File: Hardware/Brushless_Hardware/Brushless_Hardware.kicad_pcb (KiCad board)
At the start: 2 copper layers, 134.8 x 71.8 mm, 101 parts, among them J1 RJ45_LED_Shielded, SW1 SW_Push, SW2 SW_Push, SW3 SW_Push, SW4 SW_Push, SW5 SW_Push, SW6 SW_Push, SW7 SW_DPDT_x2, U1 Teensy4.1_DEV-16771, U2 OKI, U3 TSR_1-2450

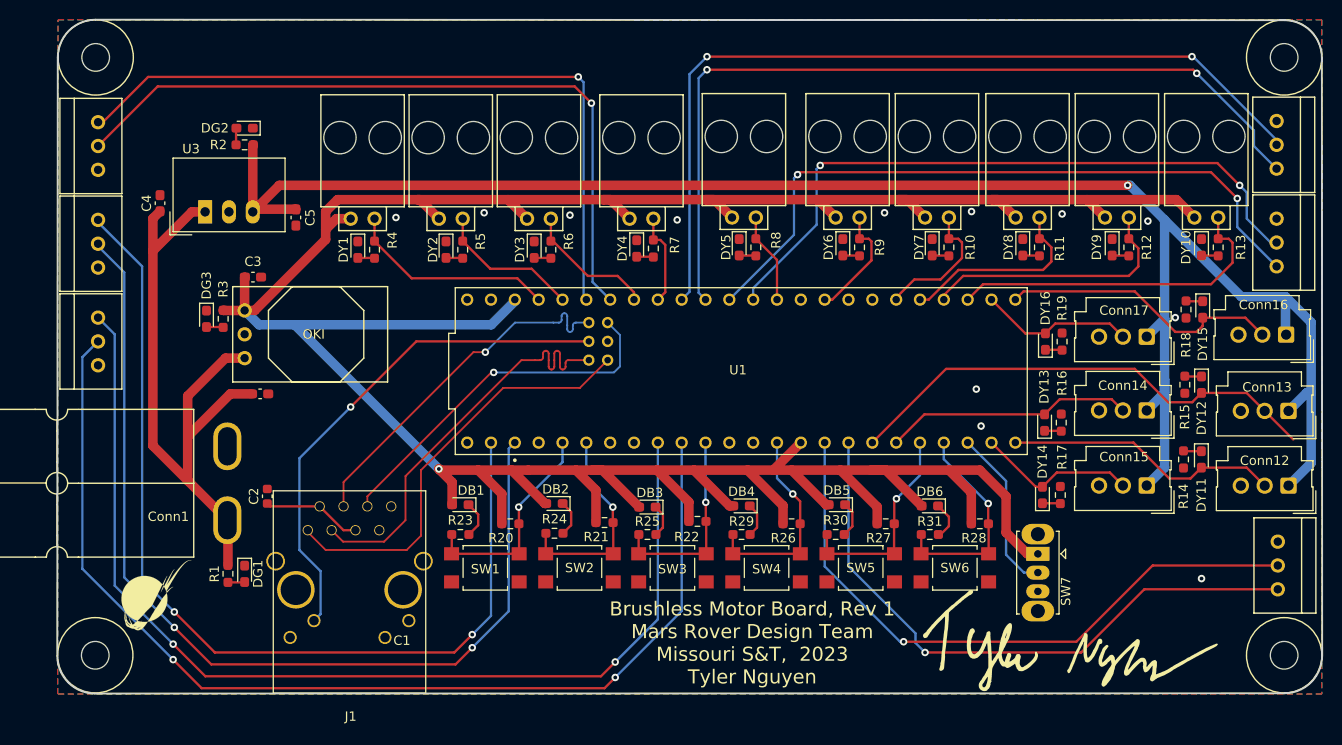
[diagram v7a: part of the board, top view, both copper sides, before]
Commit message: Replaced connectors and did more labeling
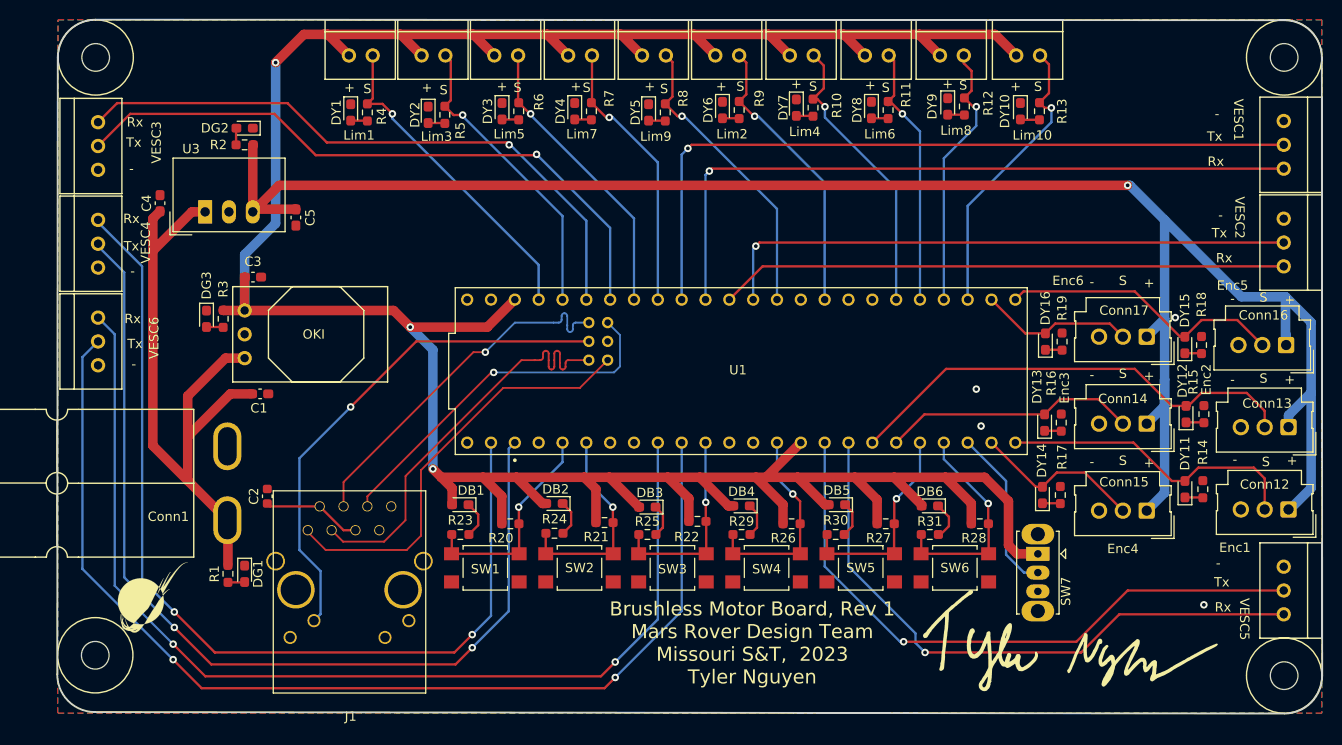
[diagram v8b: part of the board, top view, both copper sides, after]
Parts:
- Conn10, Conn11, Conn2, Conn3, Conn4, Conn5, Conn6, Conn7, Conn8, Conn9: footprint MRDT_Connectors:MOLEX_SL_02_Horizontal -> MRDT_Connectors:MOLEX_SL_02_Vertical
- moved Conn11 25.7 mm to (156.1, 28.1)
- moved Conn10 24.7 mm to (148.0, 28.1)
- moved DY10 24.1 mm to (156.6, 34.0)
- moved R13 23.9 mm to (158.6, 34.0)
- moved Conn9 23.6 mm to (140.0, 28.1)
- moved DY9 23.1 mm to (148.8, 33.5)
- moved R12 23.1 mm to (150.6, 33.5)
- moved Conn8 22.5 mm to (132.0, 28.1)
- moved DY8 21.8 mm to (140.7, 33.9)
- moved R11 21.8 mm to (142.5, 33.9)
- moved Conn7 21.5 mm to (124.1, 28.1)
- moved DY7 20.8 mm to (132.7, 33.6)
- moved R10 20.8 mm to (134.5, 33.6)
- moved Conn6 19.8 mm to (116.3, 28.1)
- moved DY6 19.5 mm to (124.8, 33.9)
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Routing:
- net LIM_9: track 9.68 -> 32.0 mm, vias 0 -> 1
- net LIM_7: track 9.91 -> 29.4 mm, vias 0 -> 1
- net LIM_2: track 12.4 -> 30.8 mm, vias 0 -> 1
- net LIM_5: track 14.3 -> 31.2 mm, vias 0 -> 1
- net LIM_3: track 15.6 -> 32.3 mm, vias 0 -> 1
- net LIM_4: track 14.5 -> 30.9 mm, vias 0 -> 1
- net VESC_Rx_1: track 91.2 -> 75.2 mm, vias 2 -> 1
- net +3.3V: track 345.4 -> 330.0 mm, vias 1 -> 3
- net VESC_Rx_2: track 73.4 -> 60.6 mm, vias 2 -> 0
- net LIM_1: track 22.5 -> 35.0 mm, vias 0 -> 1
- net VESC_Tx_1: track 91.9 -> 80.0 mm, vias 2 -> 1
- net VESC_Rx_3: track 77.7 -> 66.5 mm
- net +5V: track 193.6 -> 203.9 mm
- net VESC_Tx_3: track 78.1 -> 68.8 mm
- net VESC_Tx_2: track 71.3 -> 62.2 mm, vias 2 -> 1
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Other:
- board size 134.8 x 71.8 mm -> 134.8 x 73.9 mm
- board text added: "+"
- board text added: "-"
- board text added: "Enc1"
- board text added: "Enc2"
- board text added: "Enc3"
- board text added: "Enc4"
- board text added: "Enc5"
- board text added: "Enc6"
- board text added: "Lim1"
- board text added: "Lim10"
- board text added: "Lim2"
- board text added: "Lim3"
- board text added: "Lim4"
- board text added: "Lim5"
- board text added: "Lim6"
- board text added: "Lim7"
- board text added: "Lim8"
- board text added: "Lim9"
- board text added: "Rx"
- board text added: "S"
- board text added: "Tx"
- board text added: "VESC1"
- board text added: "VESC2"
- board text added: "VESC3"
- board text added: "VESC4"
- board text added: "VESC5"
- board text added: "VESC6"
